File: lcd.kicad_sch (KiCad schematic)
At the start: 2 parts, among them J6 687140149022, J7 687110183622

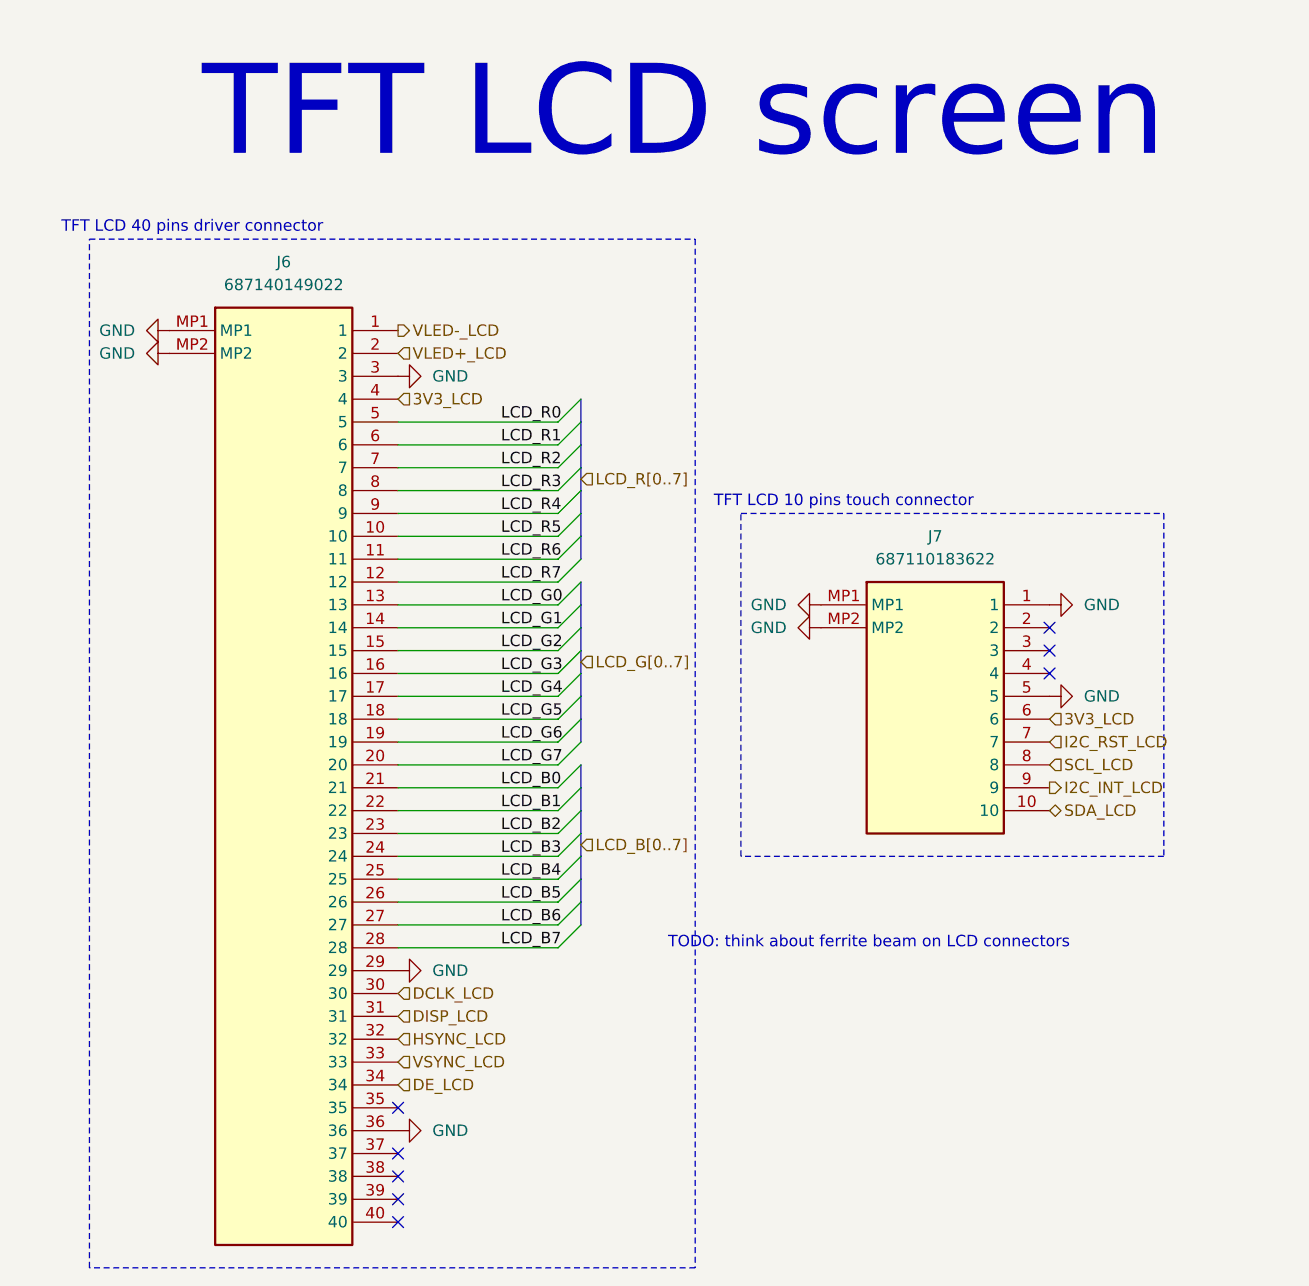
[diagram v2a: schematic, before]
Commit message: Update schematic to Kicad 10
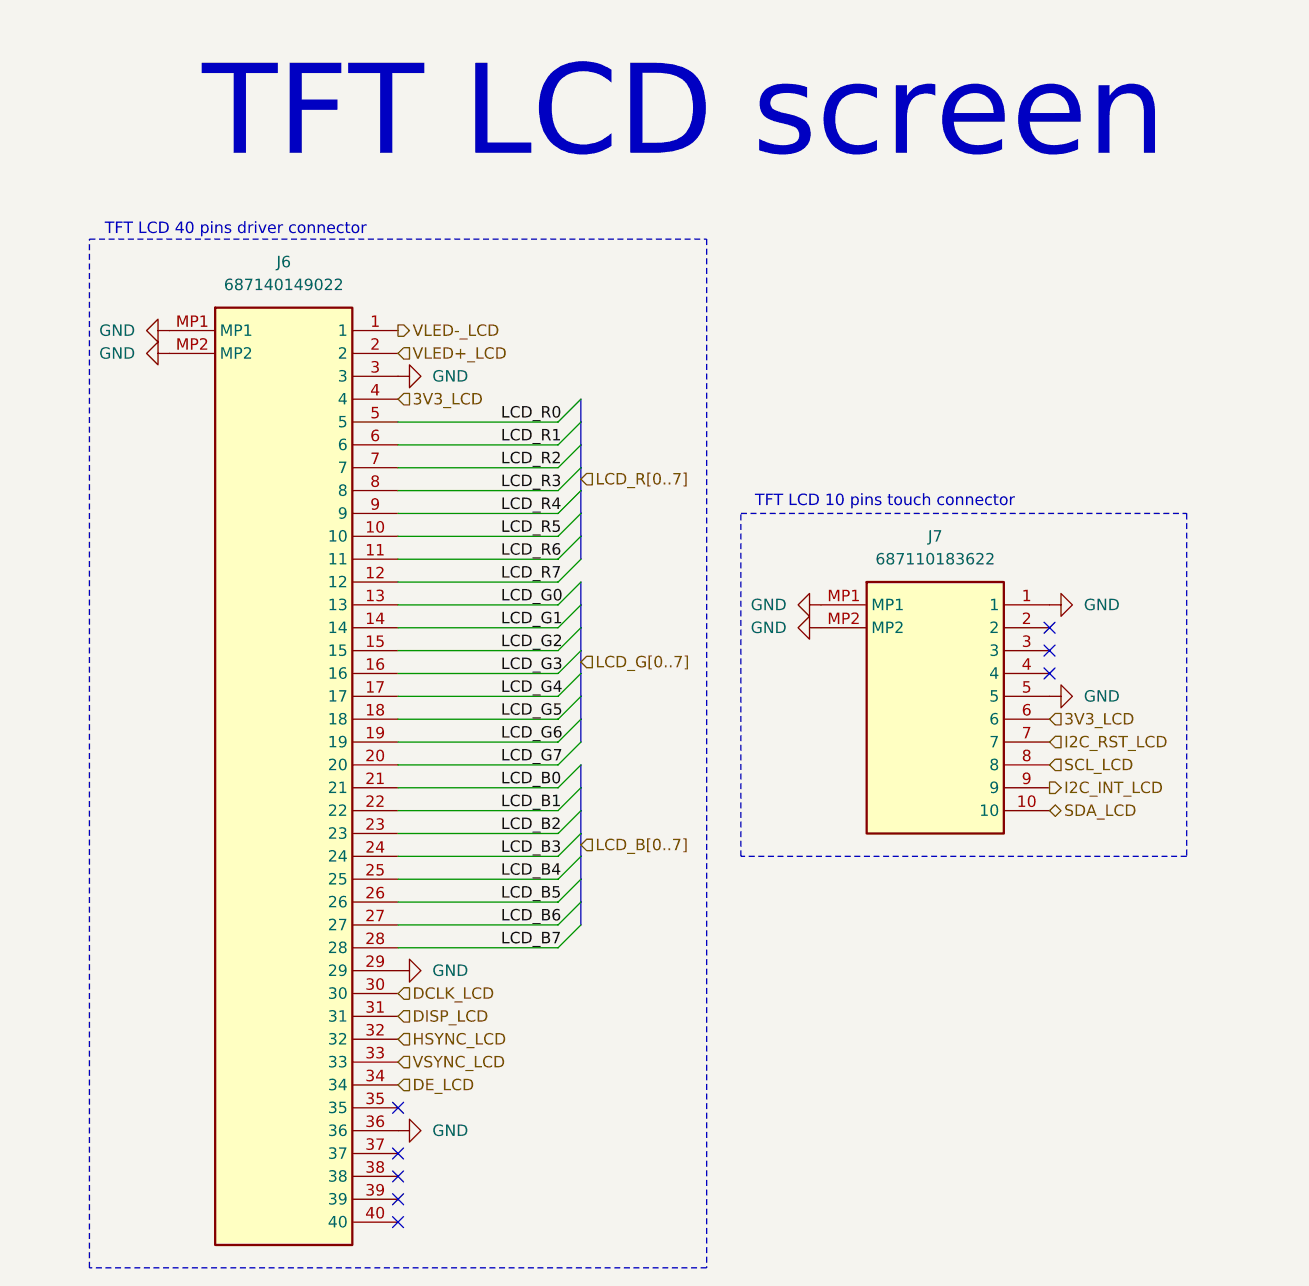
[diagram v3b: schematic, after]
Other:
- note removed: "TODO: think about ferrite beam on LCD connectors"

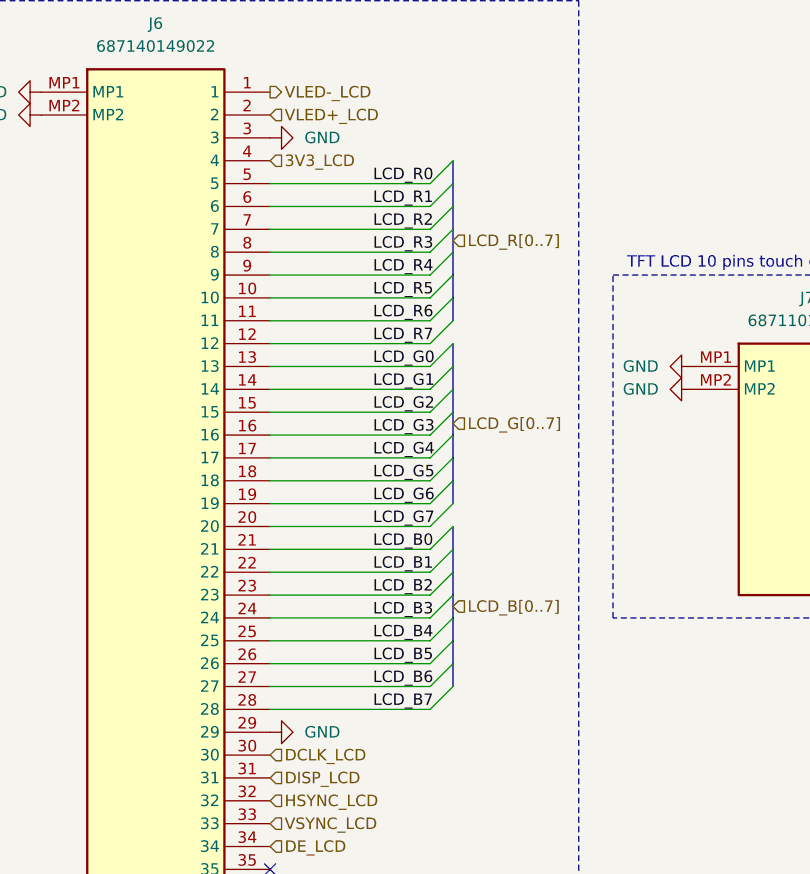
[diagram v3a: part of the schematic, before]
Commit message: Add tests points with 5015 footprint for practicity
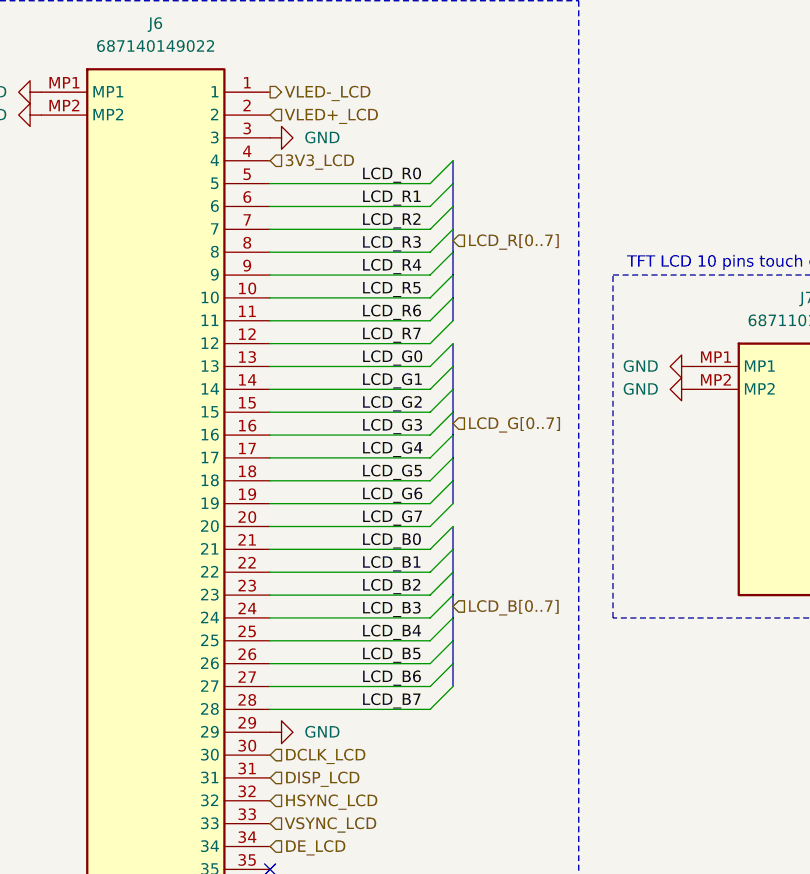
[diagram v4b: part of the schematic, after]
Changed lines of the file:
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@@
 	)
 	(label "LCD_R3"
-		(at 129.54 66.04 0)
+		(at 128.27 66.04 0)
 		(effects
 			(font
@@
 	)
 	(label "LCD_B2"
-		(at 129.54 104.14 0)
+		(at 128.27 104.14 0)
 		(effects
 			(font
@@
 	)
 	(label "LCD_B0"
-		(at 129.54 99.06 0)
+		(at 128.27 99.06 0)
 		(effects
 			(font
@@
 	)
 	(label "LCD_B1"
-		(at 129.54 101.6 0)
+		(at 128.27 101.6 0)
 		(effects
 			(font
@@
 	)
 	(label "LCD_B6"
-		(at 129.54 114.3 0)
+		(at 128.27 114.3 0)
 		(effects
 			(font
@@
 	)
 	(label "LCD_R1"
-		(at 129.54 60.96 0)
+		(at 128.27 60.96 0)
 		(effects
 			(font
@@
 	)
 	(label "LCD_R4"
-		(at 129.54 68.58 0)
+		(at 128.27 68.58 0)
 		(effects
 			(font
@@
 	)
 	(label "LCD_R6"
-		(at 129.54 73.66 0)
+		(at 128.27 73.66 0)
 		(effects
 			(font
@@
 	)
 	(label "LCD_G1"
-		(at 129.54 81.28 0)
+		(at 128.27 81.28 0)
 		(effects
 			(font
@@
 	)
 	(label "LCD_G5"
-		(at 129.54 91.44 0)
+		(at 128.27 91.44 0)
 		(effects
 			(font
@@
 	)
 	(label "LCD_G7"
-		(at 129.54 96.52 0)
+		(at 128.27 96.52 0)
 		(effects
 			(font
@@
 	)
 	(label "LCD_B4"
-		(at 129.54 109.22 0)
+		(at 128.27 109.22 0)
 		(effects
 			(font
@@
 	)
 	(label "LCD_G0"
-		(at 129.54 78.74 0)
+		(at 128.27 78.74 0)
 		(effects
 			(font
@@
 	)
 	(label "LCD_B7"
-		(at 129.54 116.84 0)
+		(at 128.27 116.84 0)
 		(effects
 			(font
@@
 	)
 	(label "LCD_G6"
-		(at 129.54 93.98 0)
+		(at 128.27 93.98 0)
 		(effects
 			(font
@@
 	)
 	(label "LCD_R7"
-		(at 129.54 76.2 0)
+		(at 128.27 76.2 0)
 		(effects
 			(font
@@
 	)
 	(label "LCD_R2"
-		(at 129.54 63.5 0)
+		(at 128.27 63.5 0)
 		(effects
 			(font
@@
 	)
 	(label "LCD_B3"
-		(at 129.54 106.68 0)
+		(at 128.27 106.68 0)
 		(effects
 			(font
@@
 	)
 	(label "LCD_B5"
-		(at 129.54 111.76 0)
+		(at 128.27 111.76 0)
 		(effects
 			(font
@@
 	)
 	(label "LCD_R5"
-		(at 129.54 71.12 0)
+		(at 128.27 71.12 0)
 		(effects
 			(font
@@
 	)
 	(label "LCD_R0"
-		(at 129.54 58.42 0)
+		(at 128.27 58.42 0)
 		(effects
 			(font
@@
 	)
 	(label "LCD_G4"
-		(at 129.54 88.9 0)
+		(at 128.27 88.9 0)
 		(effects
 			(font
@@
 	)
 	(label "LCD_G3"
-		(at 129.54 86.36 0)
+		(at 128.27 86.36 0)
 		(effects
 			(font
@@
 	)
 	(label "LCD_G2"
-		(at 129.54 83.82 0)
+		(at 128.27 83.82 0)
 		(effects
 			(font
@@
 		(dnp no)
 		(fields_autoplaced yes)
-		(property "Reference" "#PWR0117"
+		(property "Reference" "#PWR0121"
 			(at 124.46 119.38 0)
 			(hide yes)
@@
 			(project "weather-station-poc"
 				(path "/38eb53bb-294e-46e4-ad59-fd355ca373b9/887aec76-5086-421b-8a43-0ed64a6cc9fd"
-					(reference "#PWR0117")
+					(reference "#PWR0121")
 					(unit 1)
 				)
@@
 		(dnp no)
 		(fields_autoplaced yes)
-		(property "Reference" "#PWR0110"
+		(property "Reference" "#PWR0118"
 			(at 86.36 48.26 0)
 			(hide yes)
@@
 			(project "weather-station-poc"
 				(path "/38eb53bb-294e-46e4-ad59-fd355ca373b9/887aec76-5086-421b-8a43-0ed64a6cc9fd"
-					(reference "#PWR0110")
+					(reference "#PWR0118")
 					(unit 1)
 				)
@@
 		(dnp no)
 		(fields_autoplaced yes)
-		(property "Reference" "#PWR0118"
+		(property "Reference" "#PWR0122"
 			(at 124.46 137.16 0)
 			(hide yes)
@@
 			(project "weather-station-poc"
 				(path "/38eb53bb-294e-46e4-ad59-fd355ca373b9/887aec76-5086-421b-8a43-0ed64a6cc9fd"
-					(reference "#PWR0118")
+					(reference "#PWR0122")
 					(unit 1)
 				)
@@
 		(dnp no)
 		(fields_autoplaced yes)
-		(property "Reference" "#PWR0113"
+		(property "Reference" "#PWR0123"
 			(at 158.75 78.74 0)
 			(hide yes)
@@
 			(project "weather-station-poc"
 				(path "/38eb53bb-294e-46e4-ad59-fd355ca373b9/887aec76-5086-421b-8a43-0ed64a6cc9fd"
-					(reference "#PWR0113")
+					(reference "#PWR0123")
 					(unit 1)
 				)
@@
 		(dnp no)
 		(fields_autoplaced yes)
-		(property "Reference" "#PWR0115"
+		(property "Reference" "#PWR0124"
 			(at 158.75 81.28 0)
 			(hide yes)
@@
 			(project "weather-station-poc"
 				(path "/38eb53bb-294e-46e4-ad59-fd355ca373b9/887aec76-5086-421b-8a43-0ed64a6cc9fd"
-					(reference "#PWR0115")
+					(reference "#PWR0124")
 					(unit 1)
 				)
@@
 		(dnp no)
 		(fields_autoplaced yes)
-		(property "Reference" "#PWR0111"
+		(property "Reference" "#PWR0119"
 			(at 86.36 50.8 0)
 			(hide yes)
@@
 			(project "weather-station-poc"
 				(path "/38eb53bb-294e-46e4-ad59-fd355ca373b9/887aec76-5086-421b-8a43-0ed64a6cc9fd"
-					(reference "#PWR0111")
+					(reference "#PWR0119")
 					(unit 1)
 				)
@@
 		(dnp no)
 		(fields_autoplaced yes)
-		(property "Reference" "#PWR0114"
+		(property "Reference" "#PWR0125"
 			(at 196.85 78.74 0)
 			(hide yes)
@@
 			(project "weather-station-poc"
 				(path "/38eb53bb-294e-46e4-ad59-fd355ca373b9/887aec76-5086-421b-8a43-0ed64a6cc9fd"
-					(reference "#PWR0114")
+					(reference "#PWR0125")
 					(unit 1)
 				)
@@
 		(dnp no)
 		(fields_autoplaced yes)
-		(property "Reference" "#PWR0112"
+		(property "Reference" "#PWR0120"
 			(at 124.46 53.34 0)
 			(hide yes)
@@
 			(project "weather-station-poc"
 				(path "/38eb53bb-294e-46e4-ad59-fd355ca373b9/887aec76-5086-421b-8a43-0ed64a6cc9fd"
-					(reference "#PWR0112")
+					(reference "#PWR0120")
 					(unit 1)
 				)
@@
 		(dnp no)
 		(fields_autoplaced yes)
-		(property "Reference" "#PWR0116"
+		(property "Reference" "#PWR0126"
 			(at 196.85 88.9 0)
 			(hide yes)
@@
 			(project "weather-station-poc"
 				(path "/38eb53bb-294e-46e4-ad59-fd355ca373b9/887aec76-5086-421b-8a43-0ed64a6cc9fd"
-					(reference "#PWR0116")
+					(reference "#PWR0126")
 					(unit 1)
 				)
